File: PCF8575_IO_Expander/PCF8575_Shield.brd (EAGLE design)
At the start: 39.3 x 26.4 mm, 19 parts

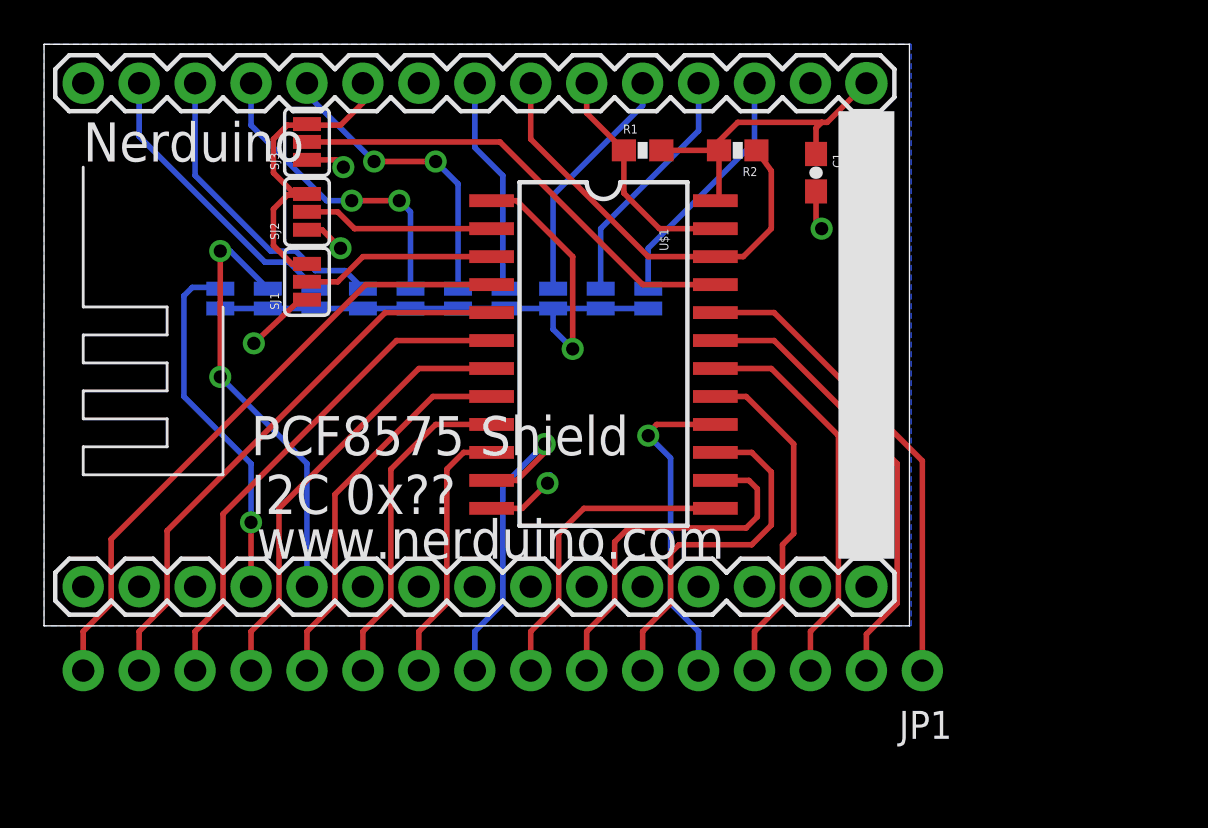
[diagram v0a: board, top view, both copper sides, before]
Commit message: Added OLED Shield Added LiPo Battery Charger Shield Updated outlines of all shields to match the cutout of the nodemcu board
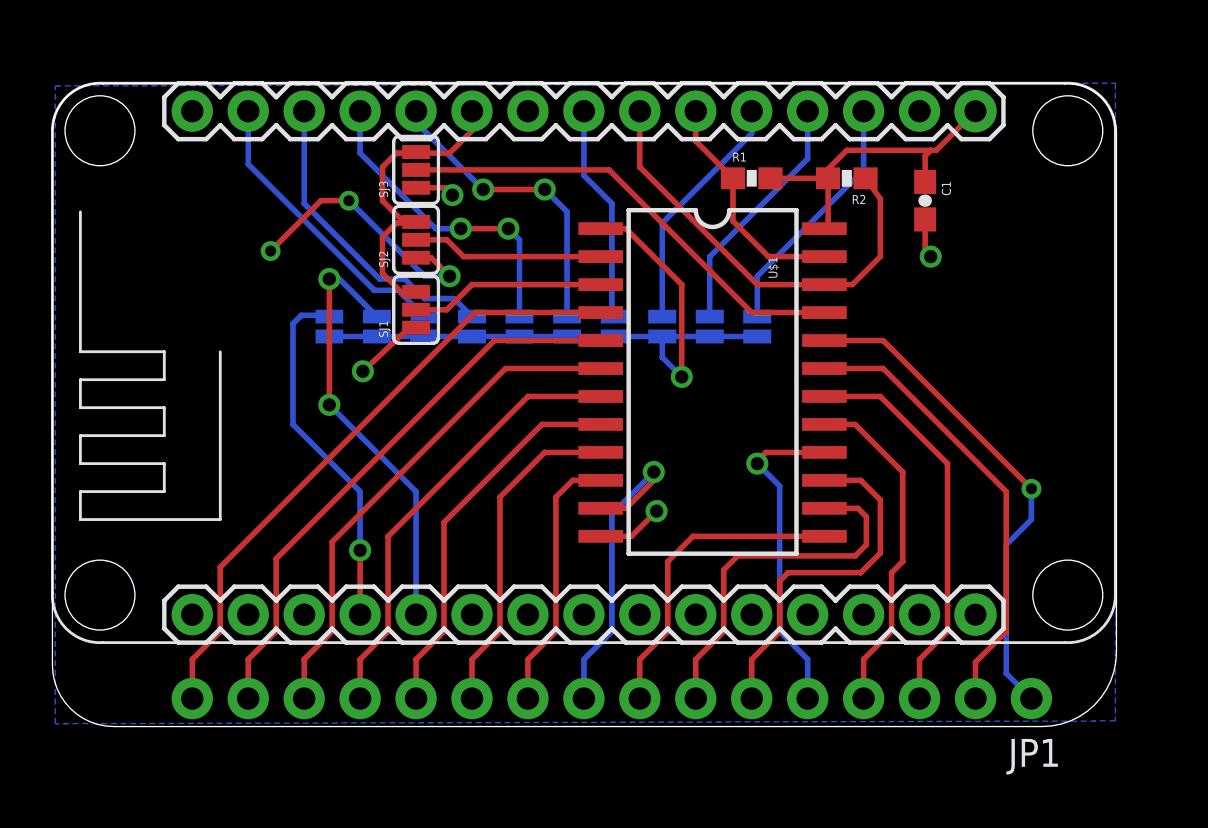
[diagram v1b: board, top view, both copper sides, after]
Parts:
- moved JP1 5.11 mm to (45.1, 1.27)
- moved C1 5.11 mm to (40.3, 23.9)
- moved R2 5.11 mm to (36.7, 24.9)
- moved SJ11 5.11 mm to (32.6, 18.2)
- moved SJ6 5.11 mm to (21.8, 18.2)
- moved SJ9 5.11 mm to (28.3, 18.2)
- moved SJ12 5.11 mm to (15.4, 18.2)
- moved R1 5.11 mm to (32.4, 24.9)
- moved SJ1 5.11 mm to (17.1, 18.9)
- moved SJ10 5.11 mm to (30.5, 18.2)
- moved SJ13 5.11 mm to (13.2, 18.2)
- moved SJ2 5.11 mm to (17.1, 22.1)
- moved SJ3 5.11 mm to (17.1, 25.3)
- moved SJ4 5.11 mm to (17.5, 18.2)
- moved SJ5 5.11 mm to (19.7, 18.2)
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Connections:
- net GND: no longer U$2.7
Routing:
- net GND: track 13.0 -> 23.7 mm, vias 5 -> 7
- net N$1: track 21.7 -> 22.7 mm, vias 0 -> 1
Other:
- board size 39.3 x 26.4 mm -> 48.3 x 29.2 mm
- board text added: "NERDUINO PCF8575 Shield I2C 0x?? www.nerduino.com"
- board text removed: "Nerduino"
- board text removed: "PCF8575 Shield I2C 0x??"
- board text removed: "www.nerduino.com"

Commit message: Updated the i2c pins to all shields to use d11/d12  as these pins will have dual use with the upcoming wifimcu Added FM24W256  Fram shield Added X95840 Digital potentiometer Shield Added AD5696 DAC Shield
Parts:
- added JP2: (no value), SparkFun:1X02
- SJ10, SJ11, SJ12, SJ13, SJ4, SJ5, SJ6, SJ7, SJ8, SJ9: value SOLDERJUMPERNO -> (none)
- moved SJ13 23.7 mm to (37.0, 18.2)
- moved SJ12 19.4 mm to (34.8, 18.2)
- moved C1 2.29 mm to (42.5, 24.0)
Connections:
- net +3V3: now also JP2.1; no longer U$2.11, U$2.25
- net GND: now also JP2.2; no longer U$2.24
- net N$2: now also U$2.5; no longer U$2.21
- net N$28: now also U$2.22; no longer U$2.20
- net N$29: now also U$2.21; no longer U$2.19
- net N$30: now also U$2.20; no longer U$2.18
- net N$31: now also U$2.19; no longer U$2.5
- net N$32: now also U$2.18; no longer U$2.4
- net N$5: now also U$2.4; no longer U$2.22
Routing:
- net N$2: track 10.5 -> 52.3 mm, vias 0 -> 2
- net N$5: track 20.0 -> 49.5 mm, vias 0 -> 2
- net +3V3: track 29.3 -> 54.3 mm
- net N$3: track 30.6 -> 45.7 mm
- net N$31: track 19.7 -> 9.38 mm, vias 2 -> 0
- net N$32: track 16.3 -> 10.3 mm, vias 1 -> 0
- net N$15: track 14.9 -> 12.4 mm
- net N$30: track 11.3 -> 9.43 mm
- net N$29: track 11.2 -> 9.59 mm
- net N$28: track 11.0 -> 9.75 mm
- net GND: track 23.7 -> 22.7 mm
- net N$19: track 20.2 -> 21.1 mm
- net N$20: track 23.1 -> 24.1 mm
- net N$21: track 25.7 -> 26.3 mm
